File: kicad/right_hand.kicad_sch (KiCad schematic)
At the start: 33 parts, among them SW34 Gateron_ks_27, SW35 Gateron_ks_27, SW36 Gateron_ks_27, SW37 Gateron_ks_27, SW38 Gateron_ks_27, SW39 Gateron_ks_27, SW40 Gateron_ks_27, SW41 Gateron_ks_27, SW42 Gateron_ks_27, SW43 Gateron_ks_27, SW44 Gateron_ks_27, SW45 Gateron_ks_27, SW46 Gateron_ks_27, SW47 Gateron_ks_27, SW48 Gateron_ks_27, SW49 Gateron_ks_27, SW50 Gateron_ks_27, SW51 Gateron_ks_27, SW52 Gateron_ks_27, SW53 Gateron_ks_27, SW54 Gateron_ks_27, SW55 Gateron_ks_27, SW56 Gateron_ks_27, SW57 Gateron_ks_27, SW58 Gateron_ks_27, SW59 Gateron_ks_27, SW60 Gateron_ks_27, SW61 Gateron_ks_27, SW62 SW_LED_DIODE, SW63 SW_LED_DIODE, SW64 SW_LED_DIODE, SW65 SW_LED_DIODE, U3 74HC595

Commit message: TMP: fixing RES and RST
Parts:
- SW34, SW35, SW36, SW37, SW38, SW39, SW40, SW41, SW42, SW43, SW44, SW45, SW46, SW47, SW48, SW49, SW50, SW51, SW52, SW53, SW54, SW55, SW56, SW57, SW58, SW59, SW60, SW61: symbol Keyboard:Gateron_ks_27 -> keyboard:Gateron_ks_27
- SW62, SW63, SW64, SW65: symbol Keyboard:SW_LED_DIODE -> keyboard:SW_LED_DIODE
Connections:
- net RST is gone; now on net 5V: U3.10 (~{SRCLR})

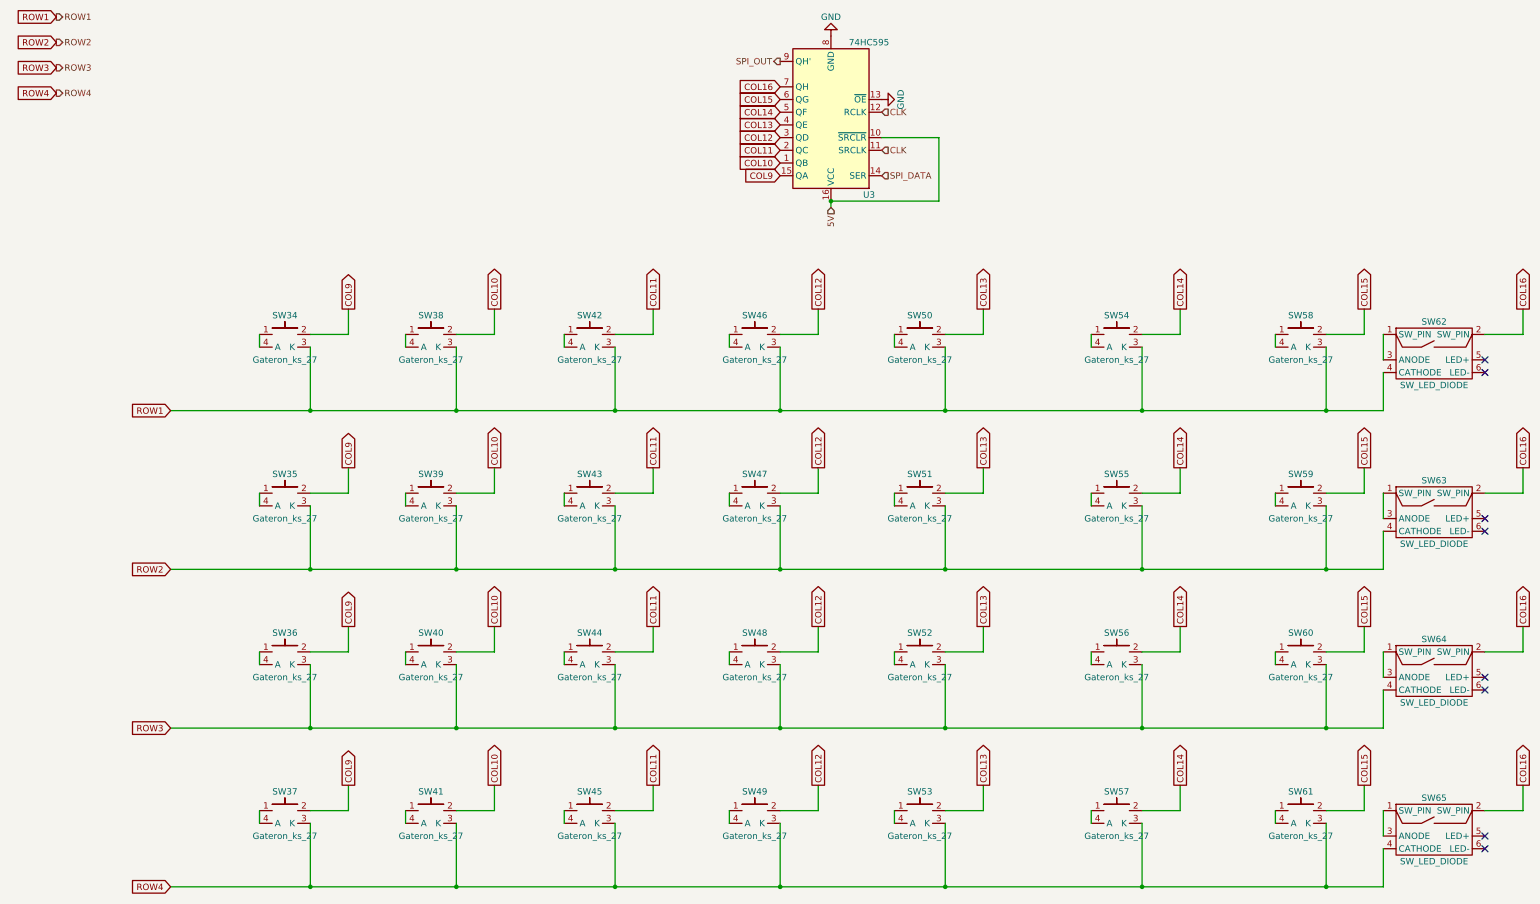
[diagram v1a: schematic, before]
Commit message: TMP: remove unused stuff
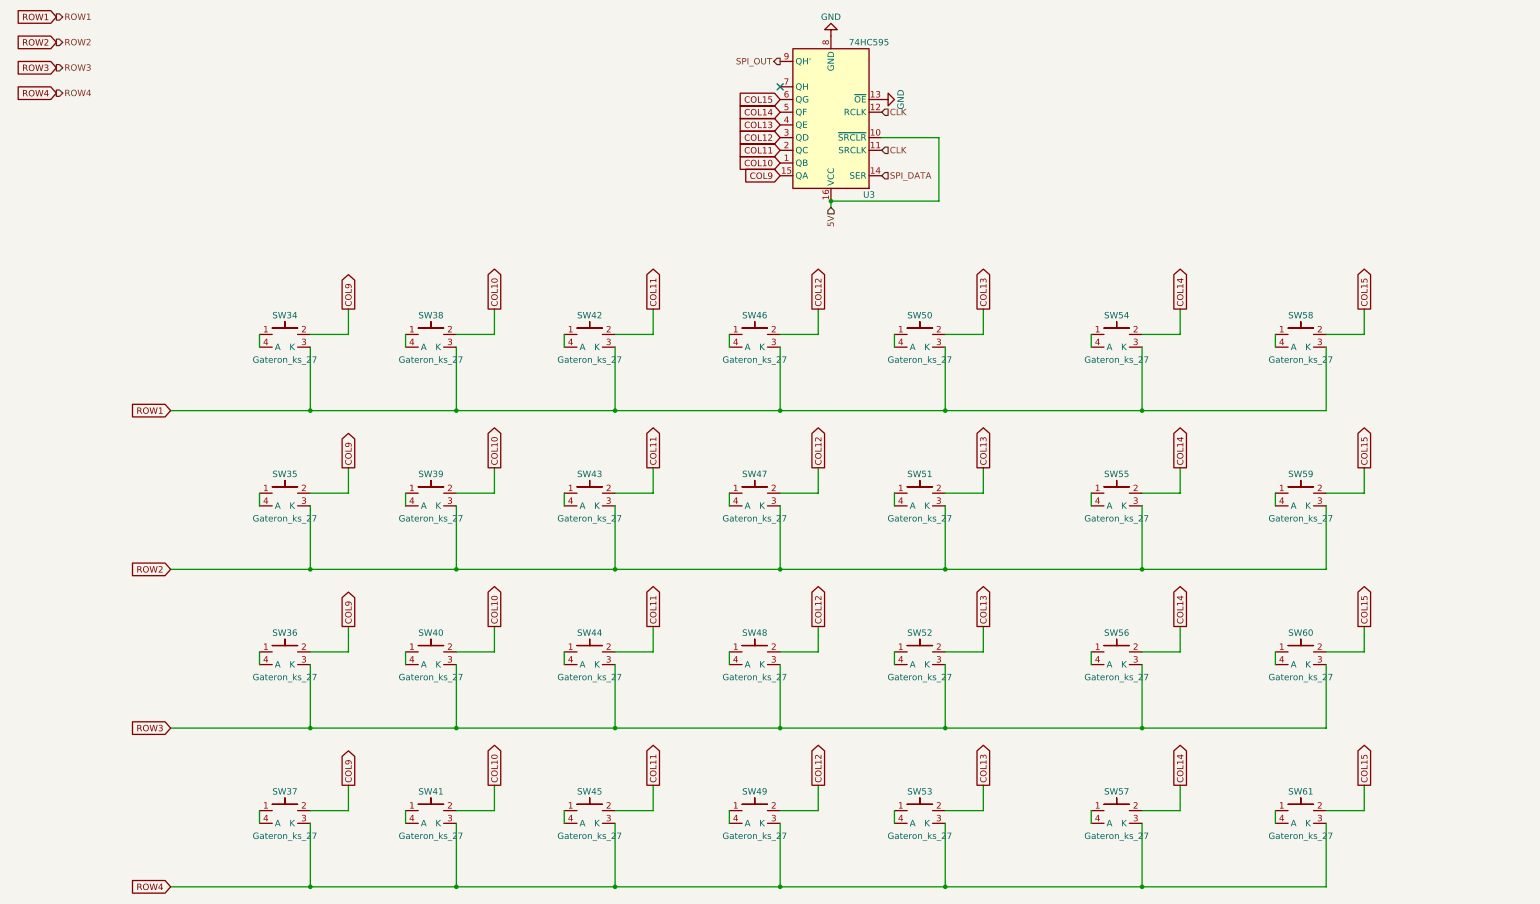
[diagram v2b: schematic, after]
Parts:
- removed SW62, SW63, SW64, SW65: SW_LED_DIODE, Keyboard:SW_LED_ext_DIODE, symbol keyboard:SW_LED_DIODE
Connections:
- net COL16: no longer names the net of U3.7 (QH)
- no-connect marks 8 -> 1
